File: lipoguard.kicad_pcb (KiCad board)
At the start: 2 copper layers, 13 parts, among them P1 CONN_2, P2 CONN_2, U1 BTS6143, U2 LM358

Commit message: Finished cleaning up
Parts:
- removed D3: ZENER, discret:D3
- removed R5: R, libcms:SM0603
- removed U2: LM358, smd_dil:so-8
- added Q1: BC 850C, misc:sot23BEC, F.Cu at (155.6, 73.0)
- added RV1: 10k, misc:trimmer1, F.Cu at (146.1, 81.3)
- C1: value C -> 100nf
- R3: footprint discret:R3 -> libcms:SM0603
- R4: value R -> 4.7k
- moved D2 40.9 mm to (156.2, 67.9), turned to 0 degrees
- moved D1 40.0 mm to (156.2, 66.0), turned to 0 degrees
- moved R2 39.3 mm to (153.0, 67.9), turned to 0 degrees
- moved R3 37.5 mm to (156.2, 70.5), turned to 0 degrees
- moved U1 35.5 mm to (141.0, 71.8), turned to 90 degrees
- moved R1 35.4 mm to (153.0, 66.0), turned to 0 degrees
- moved P2 31.9 mm to (162.6, 73.7)
- moved C1 26.5 mm to (154.3, 77.5), turned to 0 degrees
- moved P1 26.3 mm to (130.8, 74.3)
- moved R4 25.3 mm to (154.3, 75.6), turned to 0 degrees
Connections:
- C1 pad 1: VCC -> Net-(C1-Pad1)
- R4 pad 1: VCC -> Net-(C1-Pad1)
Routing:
- net Net-(P2-Pad2): track 44.5 -> 22.8 mm, vias 0 -> 30
- net Net-(Q1-Pad3): track 26.3 -> 6.95 mm, vias 2 -> 0
- net Net-(D3-Pad2): track 13.2 -> 0.00 mm
- net Net-(C1-Pad1): track 0.00 -> 12.1 mm
- net Net-(R3-Pad1): track 3.43 -> 7.88 mm
- net VCC: track 42.9 -> 44.8 mm, vias 0 -> 33
- net Net-(D2-Pad1): track 2.29 -> 1.65 mm
- net Net-(D1-Pad1): track 2.29 -> 1.65 mm
- added copper zone on B.Cu, net GND
- added copper zone on B.Cu, net Net-(P2-Pad2)
- added copper zone on F.Cu, net Net-(P2-Pad2)
- added copper zone on B.Cu, net VCC
- added copper zone on F.Cu, net VCC
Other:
- board outline added: 39.4 x 19.7 mm
- rule via_min_drill: 0.3 -> 0.2
- board text removed: "Lipoguard"

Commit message: Cleaned up pcb
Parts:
- added G***: LOGO, misc:logo, B.Cu at (153.0, 73.7)

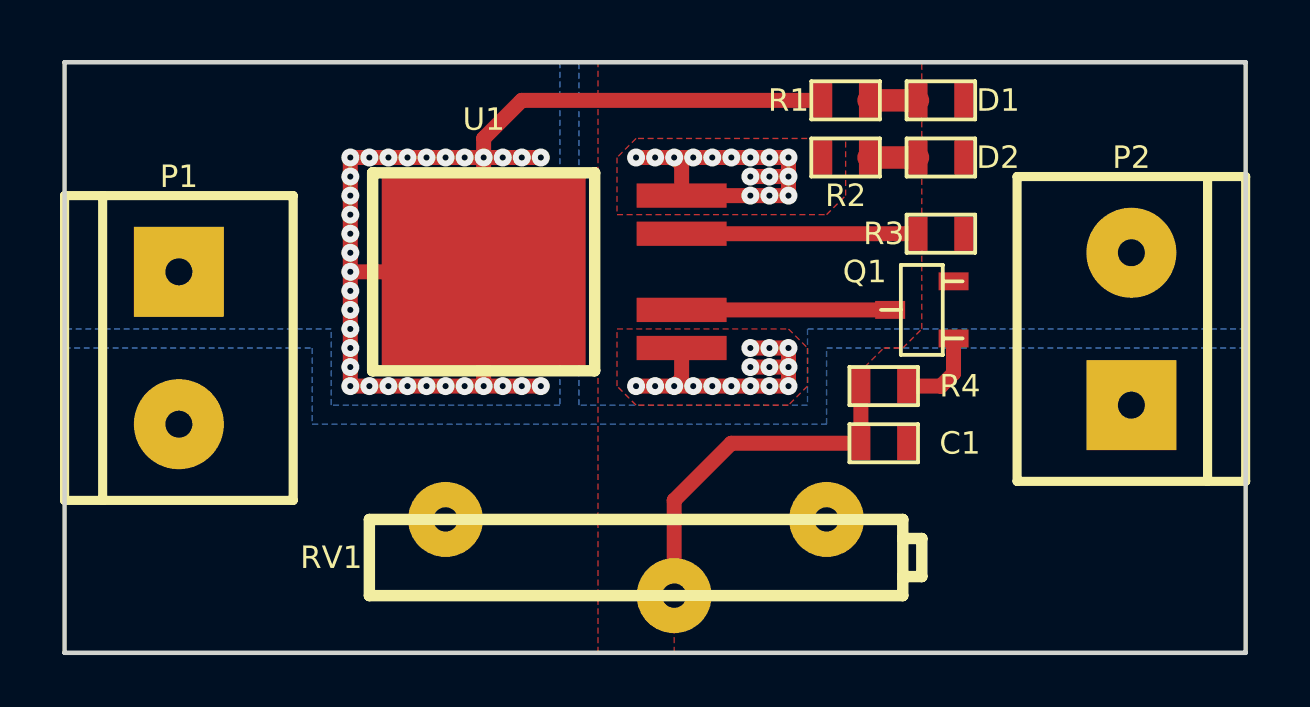
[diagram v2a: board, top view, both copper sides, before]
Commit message: Used smaller Logo
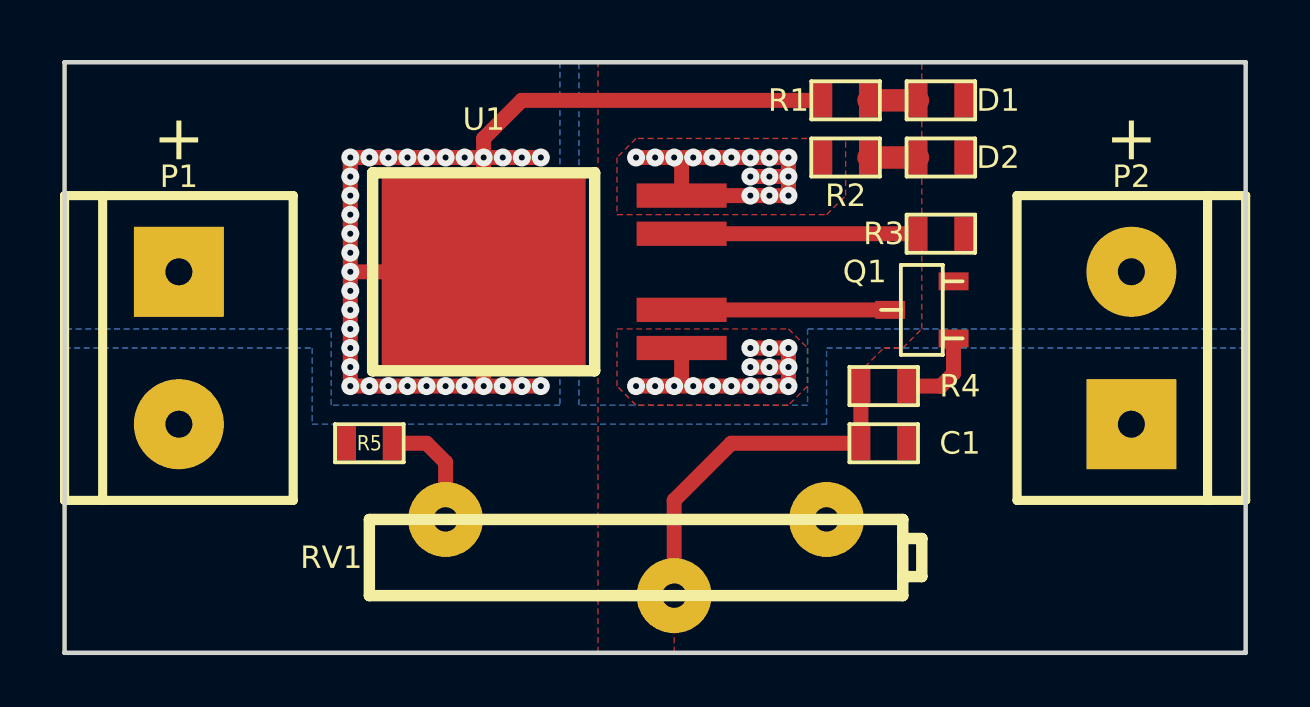
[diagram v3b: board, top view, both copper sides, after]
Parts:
- removed the G*** at (153.0, 73.7)
- added G***: logo_hacker_silkbot_10_00mm, misc:logo_hacker_silkbot_10_00mm, B.Cu at (144.1, 72.4)
- added R5: 10k, libcms:SM0603, F.Cu at (137.2, 77.5)
- RV1: value 10k -> 5k
- moved P2 0.64 mm to (162.6, 74.3)
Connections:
- RV1 pad 3: VCC -> Net-(R5-Pad2)
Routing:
- net Net-(R5-Pad2): track 0.00 -> 3.95 mm
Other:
- board text added: "+"
- board text added: "LiPo Guard"
- board text added: "Version 1.0 by Sebastian Schumb 2016"

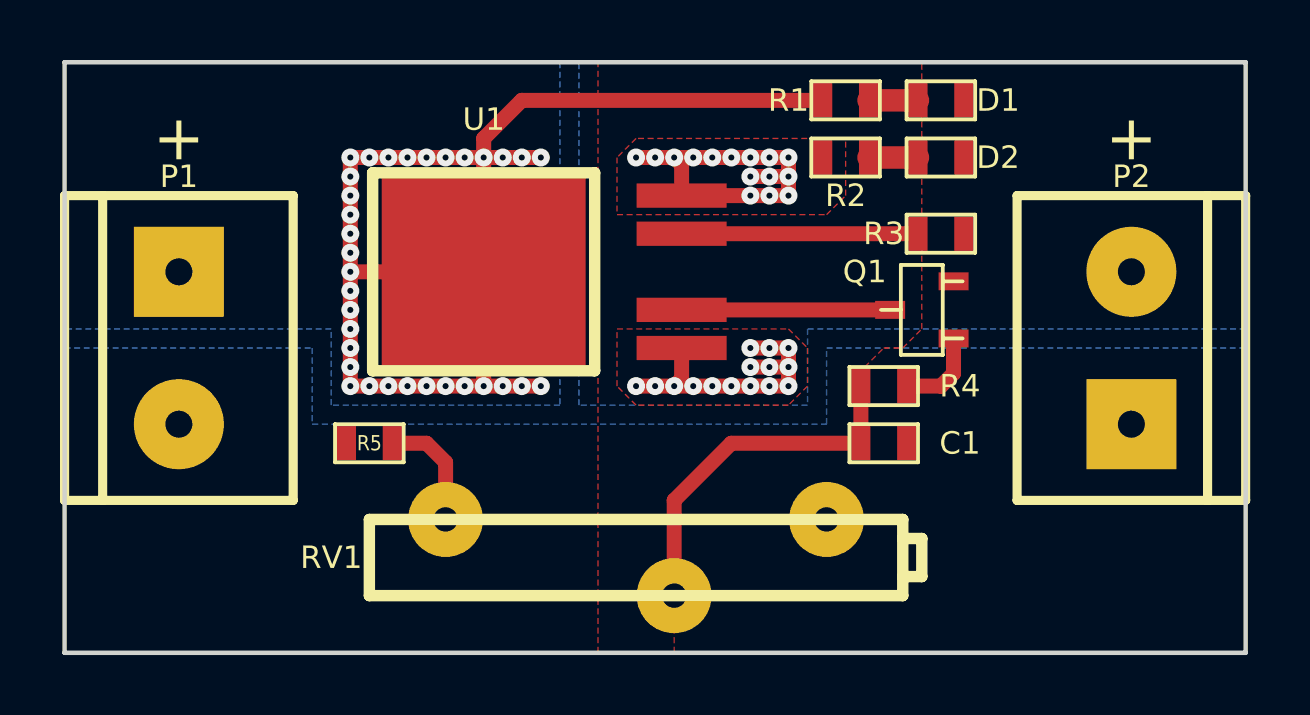
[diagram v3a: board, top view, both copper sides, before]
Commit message: Enhanced silkscreen
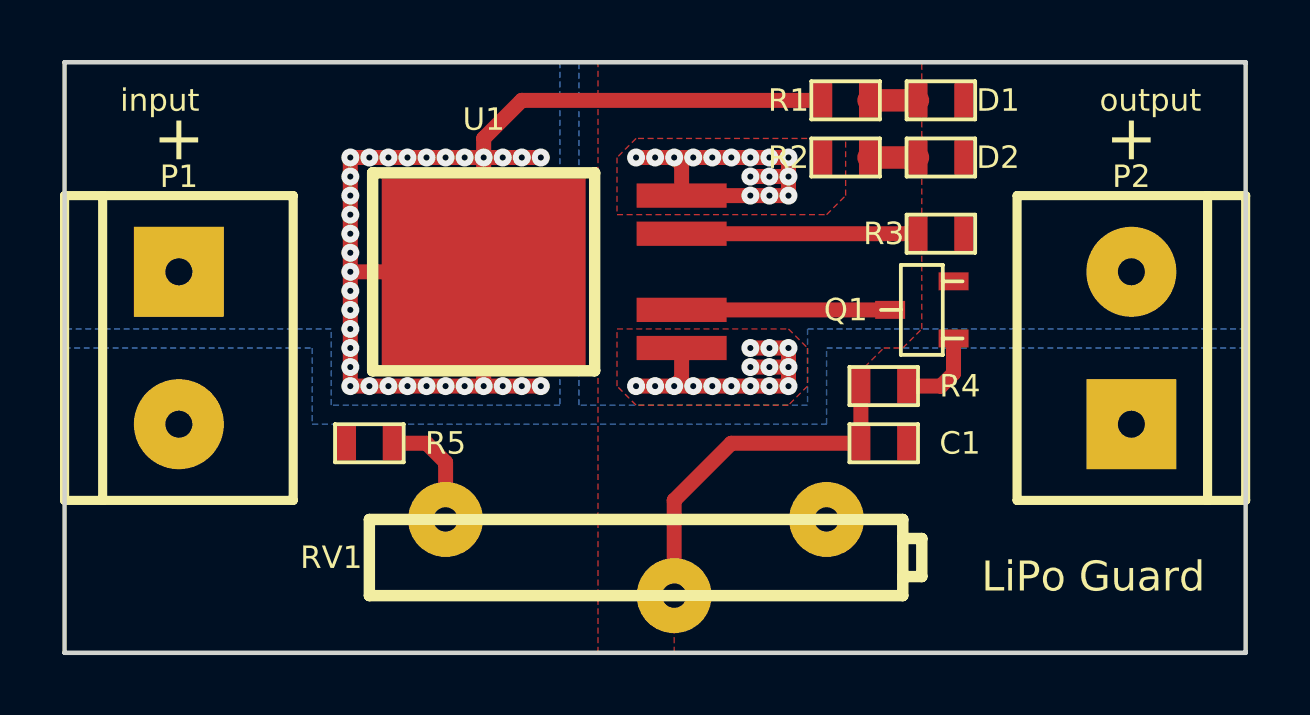
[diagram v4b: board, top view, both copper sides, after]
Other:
- board text added: "+10 on night vision"
- board text added: "24V 5A"
- board text added: "CC-BY-SA 3.0"
- board text added: "Magic smoke refills sold seperately"
- board text added: "Prevents up to 80% of all spontaneous combustions"
- board text added: "https://github.com/LongHairedHacker/LipoGuard"
- board text added: "input"
- board text added: "output"
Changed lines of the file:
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@@
     (area 126.924999 64.694999 166.445001 84.530001)
     (thickness 1.6)
-    (drawings 10)
+    (drawings 19)
     (tracks 148)
     (zones 0)
@@
   )
   (setup
-    (last_trace_width 0.5)
+    (last_trace_width 0.25)
     (user_trace_width 0.5)
     (user_trace_width 0.75)
@@
     (visible_elements FFFFFF7F)
     (pcbplotparams
-      (layerselection 0x01030_80000001)
+      (layerselection 0x010f0_80000001)
       (usegerberextensions true)
       (excludeedgelayer true)
@@
     (at 153.035 67.945)
     (attr smd)
-    (fp_text reference R2 (at 0 1.27) (layer F.SilkS)
+    (fp_text reference R2 (at -1.905 0) (layer F.SilkS)
       (effects (font (size 0.75 0.75) (thickness 0.15)))
     )
@@
     (descr SOT23)
     (attr smd)
-    (fp_text reference Q1 (at 1.27 -1.905 180) (layer F.SilkS)
+    (fp_text reference Q1 (at 0 -2.54 180) (layer F.SilkS)
       (effects (font (size 0.75 0.75) (thickness 0.15)))
     )
@@
     (at 137.16 77.47)
     (attr smd)
-    (fp_text reference R5 (at 0 0) (layer F.SilkS)
-      (effects (font (size 0.508 0.4572) (thickness 0.1143)))
+    (fp_text reference R5 (at 2.54 0) (layer F.SilkS)
+      (effects (font (size 0.75 0.75) (thickness 0.15)))
     )
     (fp_text value 10k (at 0 0) (layer F.SilkS) hide
@@
       (xy 0.14224 2.76098) (xy 0.14224 2.75336) (xy 0.14224 2.74066) (xy 0.14224 2.74066)) (layer B.SilkS) (width 0.00254))
   )
-  (gr_text "Version 1.0 \nby Sebastian Schumb \n2016" (at 158.75 81.915) (layer B.SilkS)
+  (gr_text output (at 163.195 66.04) (layer F.SilkS)
+    (effects (font (size 0.75 0.75) (thickness 0.15)))
+  )
+  (gr_text input (at 130.175 66.04) (layer F.SilkS)
+    (effects (font (size 0.75 0.75) (thickness 0.15)))
+  )
+  (gr_text "LiPo Guard" (at 161.29 81.915) (layer F.SilkS)
+    (effects (font (size 1 1) (thickness 0.15)))
+  )
+  (gr_text "CC-BY-SA 3.0" (at 140.97 82.55 7) (layer B.SilkS)
     (effects (font (size 0.75 0.75) (thickness 0.15)) (justify mirror))
   )
+  (gr_text "+10 on night vision" (at 146.685 78.74 7) (layer B.SilkS)
+    (effects (font (size 0.65 0.65) (thickness 0.1625)) (justify mirror))
+  )
+  (gr_text https://github.com/LongHairedHacker/LipoGuard (at 139.7 66.675 5) (layer B.SilkS)
+    (effects (font (size 0.65 0.65) (thickness 0.15)) (justify mirror))
+  )
+  (gr_text "24V\n5A" (at 154.305 70.485) (layer B.SilkS)
+    (effects (font (size 1 1) (thickness 0.25)) (justify mirror))
+  )
+  (gr_text "Prevents up to 80% of all\nspontaneous combustions" (at 135.89 75.565 80) (layer B.SilkS)
+    (effects (font (size 0.75 0.75) (thickness 0.15)) (justify mirror))
+  )
+  (gr_text "Magic smoke refills \nsold seperately" (at 154.94 74.295 33) (layer B.SilkS)
+    (effects (font (size 0.75 0.75) (thickness 0.15)) (justify mirror))
+  )
+  (gr_text "Version 1.0 \nby Sebastian Schumb \n2016" (at 158.75 81.915 10) (layer B.SilkS)
+    (effects (font (size 0.75 0.75) (thickness 0.15)) (justify mirror))
+  )
